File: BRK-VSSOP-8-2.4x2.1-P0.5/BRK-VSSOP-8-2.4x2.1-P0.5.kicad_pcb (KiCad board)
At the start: 2 copper layers, 18.3 x 22.6 mm, 3 parts, among them J1 Conn_01x04, J2 Conn_01x04, U1 VSSOP-8-2.4x2.1-P0.5

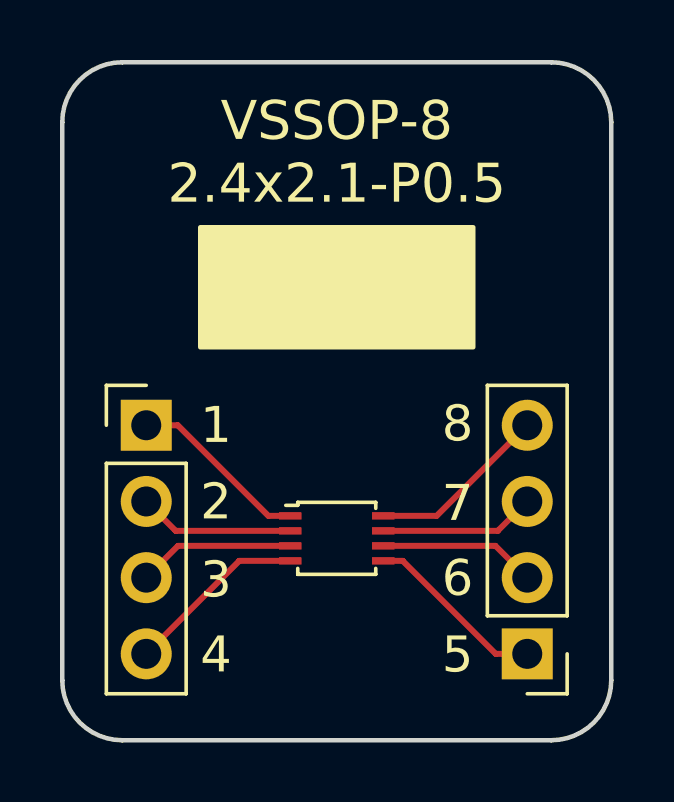
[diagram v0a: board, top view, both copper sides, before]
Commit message: Update several breakout boards
* Reduce distance from edge to pin header
* Enlarge silk screen area
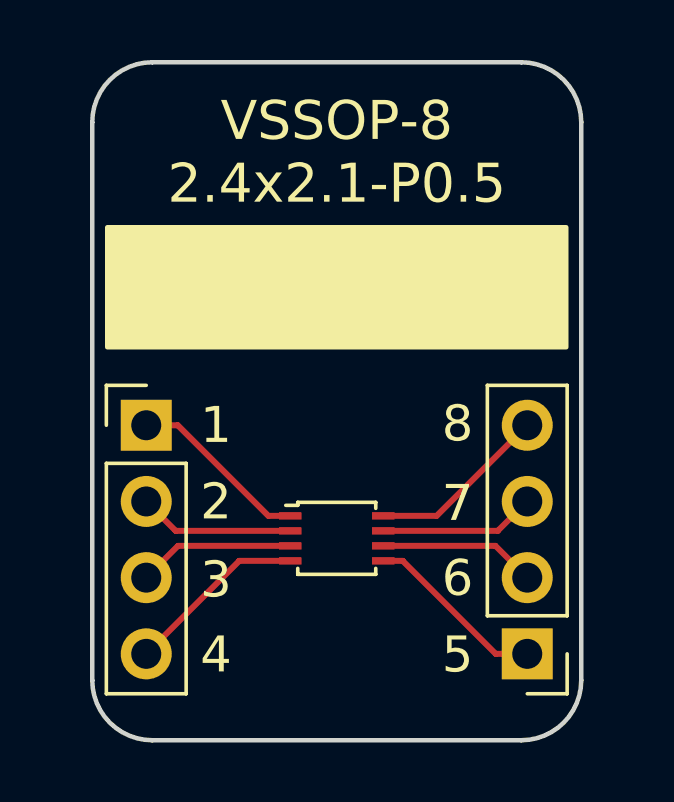
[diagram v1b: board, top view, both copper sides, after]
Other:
- board size 18.3 x 22.6 mm -> 16.3 x 22.6 mm
